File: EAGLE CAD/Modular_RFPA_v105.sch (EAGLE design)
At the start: 197 parts, among them IC201 74AHC1G14DBV, IC202 LM324D, J1 FUSE_2P, J2 KK_PCFAN, Q1 IRF540, Q101 IRF630, Q102 IRF520N, Q2 IRF540, Q201 BSS123, T1 HP4_TRAFO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

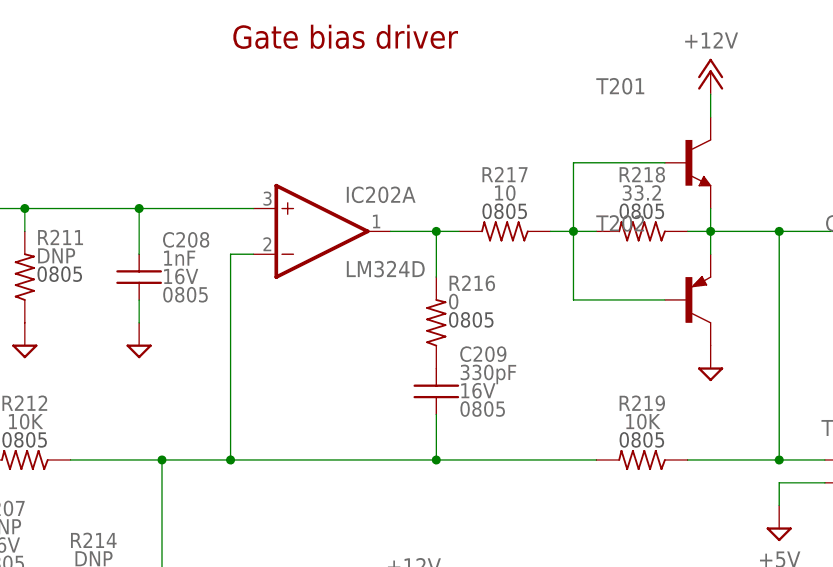
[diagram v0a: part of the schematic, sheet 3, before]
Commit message: change a couple bias driver components
need to rework the 01 board like this too
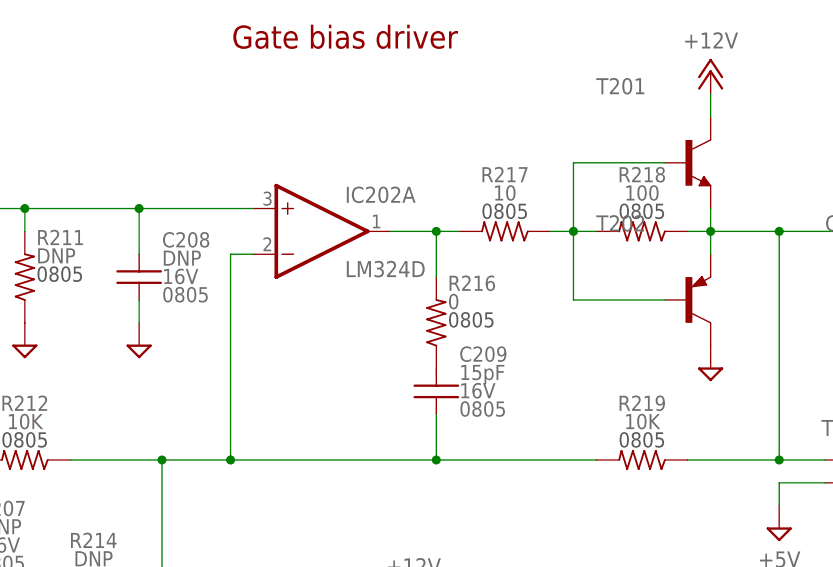
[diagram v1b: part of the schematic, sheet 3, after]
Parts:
- C208: value 1nF -> DNP
- C209: value 330pF -> 15pF
- R218: value 33.2 -> 100
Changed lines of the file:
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@@
 </attributes>
 <variantdefs>
-<variantdef name="IRF520N_20W"/>
+<variantdef name="IRF520N_20W" current="yes"/>
 <variantdef name="IRF630_200W"/>
 </variantdefs>
@@
 <part name="R117" library="MDT_R" deviceset="R" device="R2512" technology="R-1K-1%-2512-1W" value="330">
 <variant name="IRF520N_20W" value="2.74K"/>
-<variant name="IRF630_200W" value="117"/>
 </part>
 <part name="R113" library="MDT_R" deviceset="R" device="0805_IPC" technology="R-1.0K-0.1%-0805-0.1W" value="15"/>
@@
 <part name="R209" library="MDT_R" deviceset="R" device="0805_IPC" technology="R-1.0K-0.1%-0805-0.1W" value="1.0K"/>
 <part name="R217" library="MDT_R" deviceset="R" device="0805_IPC" technology="R-1.0K-0.1%-0805-0.1W" value="10"/>
-<part name="R218" library="MDT_R" deviceset="R" device="0805_IPC" technology="R-1.0K-0.1%-0805-0.1W" value="33.2"/>
+<part name="R218" library="MDT_R" deviceset="R" device="0805_IPC" technology="R-1.0K-0.1%-0805-0.1W" value="100"/>
 <part name="R219" library="MDT_R" deviceset="R" device="0805_IPC" technology="R-1.0K-0.1%-0805-0.1W" value="10K"/>
 <part name="R212" library="MDT_R" deviceset="R" device="0805_IPC" technology="R-1.0K-0.1%-0805-0.1W" value="10K"/>
@@
 <part name="R206" library="MDT_R" deviceset="R" device="0805_IPC" technology="R-1.0K-0.1%-0805-0.1W" value="10K"/>
 <part name="R205" library="MDT_R" deviceset="R" device="0805_IPC" technology="R-1.0K-0.1%-0805-0.1W" value="10K"/>
-<part name="C209" library="MDT_C" deviceset="C" device="0805_IPC" technology="C-0.1U-16V-0805-X7R" value="330pF"/>
+<part name="C209" library="MDT_C" deviceset="C" device="0805_IPC" technology="C-0.1U-16V-0805-X7R" value="15pF"/>
 <part name="R216" library="MDT_R" deviceset="R" device="0805_IPC" technology="R-1.0K-0.1%-0805-0.1W" value="0"/>
 <part name="C207" library="MDT_C" deviceset="C" device="0805_IPC" technology="C-0.1U-16V-0805-X7R" value="DNP">
@@
 <variant name="IRF630_200W" populate="no"/>
 </part>
-<part name="C208" library="MDT_C" deviceset="C" device="0805_IPC" technology="C-0.1U-16V-0805-X7R" value="1nF"/>
+<part name="C208" library="MDT_C" deviceset="C" device="0805_IPC" technology="C-0.1U-16V-0805-X7R" value="DNP">
+<variant name="IRF520N_20W" populate="no"/>
+<variant name="IRF630_200W" populate="no"/>
+</part>
 <part name="C201" library="MDT_C" deviceset="C" device="0805_IPC" technology="C-0.1U-16V-0805-X7R" value="0.1uF"/>
 <part name="C210" library="MDT_C" deviceset="C" device="0805_IPC" technology="C-0.1U-16V-0805-X7R" value="0.1uF"/>

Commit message: More schematic editing
Add DR127 to my library
More assembly variant component values
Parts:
- C1, C7: value 22nF -> 2.2nF
- C11, C5: value 0.1uF -> 27nF
- C12, C6: value 0.1uF -> 22nF
- C2, C8: value 0.1uF -> 10nF
- L1, L2: value 1uH -> 47nH
- L6: value 22uH -> (none); device inductors:DR127 -> MDT_L:L
- L7: value DR127 -> (none); device inductors:DR127 -> MDT_L:L
- Q1, Q2: value IRF540 -> IRF630
- R1, R14: value 1K -> 270
- R12, R25: value 1.0K -> 100
- R13, R18, R26, R5: value 1K -> 75
- R15, R16, R2, R3, R36, R38: value 1K -> 2.7
- R17, R4: value 1K -> 100
- R19, R6: value 1K -> 4.99
- R20, R7: value 1K -> 330
- R21, R8: value 1.0K -> 15
- R37, R39: value 1K -> 3.3

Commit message: Work on libraries...
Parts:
- C1, C111, C112, C7: value 2.2nF -> 22nF
- C102, C104, C12, C6: value 22nF -> 0.1uF
- C103, C11, C5: value 27nF -> 0.1uF
- C105: value 12nF -> 0.1uF
- C106, C107, C109, C110, C17, C207, C208, C24, C26, C27, C28: value DNP -> 0.1uF
- C113, C114, C2, C8: value 10nF -> 0.1uF
- C15, C16: value 4.7uF -> 47nF
- C209: value 15pF -> 0.1uF
- C25: value 1.5nF -> 0.1uF
- C29: value 100nF -> 0.1uF
- L1, L101, L2: value 47nH -> 1uH
- L102: value 150nH -> 1uH
- L4, L5: device inductors:DR127 -> MDT_L:L
- R1, R118, R120, R14: value 270 -> 1K
- R101, R105, R13, R18, R26, R5: value 75 -> 1K
- R102, R106: value 150 -> 1K
- R103, R19, R6: value 4.99 -> 1K
- R104: value 10 -> 1K
- R107, R109, R12, R218, R25: value 100 -> 1.0K
- R108, R110, R17, R4: value 100 -> 1K
- R111, R112, R115, R116, R211, R214: value DNP -> 1.0K
- R113, R114, R21, R8: value 15 -> 1.0K
- R117, R20, R7: value 330 -> 1K
- R119: value 2.74K -> 1K
- R121, R123, R15, R16, R2, R3, R34, R36, R38: value 2.7 -> 1K
- R122, R124: value 6.8 -> 1K
- R202, R203, R204, R205, R206, R212, R219: value 10K -> 1.0K
- R216, R30: value 0 -> 1.0K
- R217: value 10 -> 1.0K
- R302, R303, R40: value 1.0 -> 1K
- R32, R33: value 8.2 -> 1K
- R35, R37, R39: value 3.3 -> 1K
- R41: value 150 -> 1.0K
- R43: value 0.5 -> 1K
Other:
- moved on the sheet: C14, C16, C19, C20, C21, C30, C301, D2, D301, H1, H2, H3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
